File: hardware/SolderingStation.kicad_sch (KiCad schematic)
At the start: 10 parts, among them J1 AC Screw Terminal, J2 Iron Encoder, J3 Hot Air Encoder, J4 OLED, J5 STM32 SWD, J6 ESP UART, J7 STM BOOT, J8 +5V

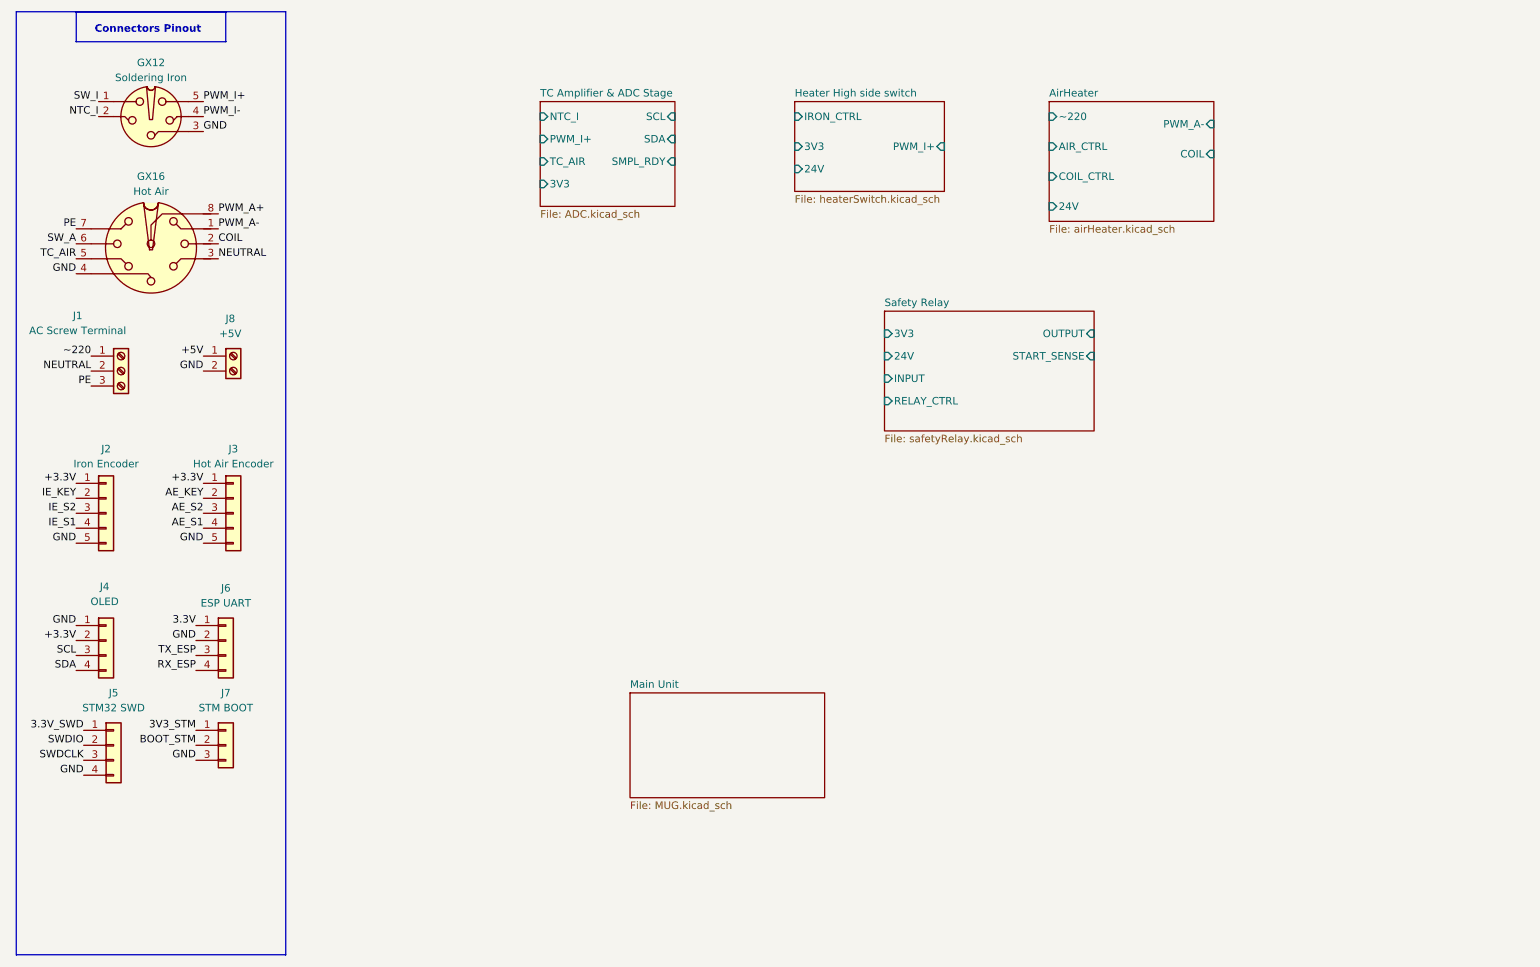
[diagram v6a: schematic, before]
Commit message: mvp
features:
	Logic Power Supply
	Safety Relay
	Main Unit
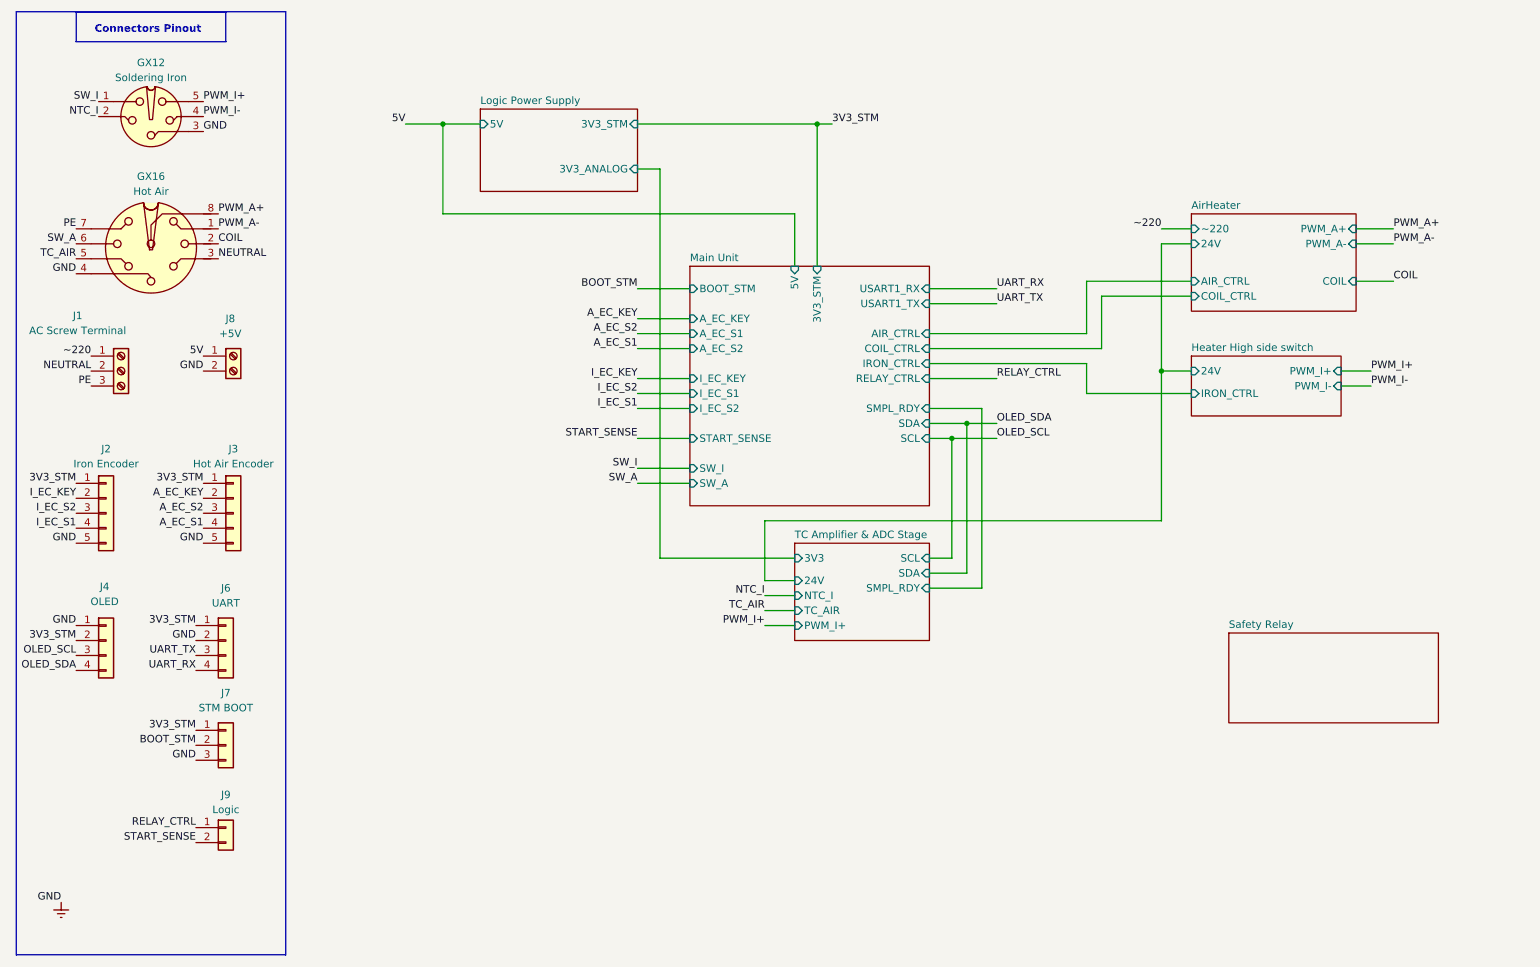
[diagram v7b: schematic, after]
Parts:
- removed J5: STM32 SWD, symbol Connector_Generic:Conn_01x04
- added J9: Logic, symbol Connector_Generic:Conn_01x02
- J6: value ESP UART -> UART
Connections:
- net +3.3V is gone; now on net 3V3_STM: J2.1 (Pin_1), J3.1 (Pin_1), J4.2 (Pin_2)
- net 3.3V is gone; now on net 3V3_STM: J6.1 (Pin_1)
- net +5V renamed 5V
- net AE_KEY renamed A_EC_KEY
- net AE_S1 renamed A_EC_S1
- net AE_S2 renamed A_EC_S2
- net GND renamed GNDREF
- net IE_KEY renamed I_EC_KEY
- net IE_S1 renamed I_EC_S1
- net IE_S2 renamed I_EC_S2
- net RX_ESP renamed UART_RX
- net SCL renamed OLED_SCL
- net SDA renamed OLED_SDA
- net TX_ESP renamed UART_TX
- new net RELAY_CTRL: J9.1 (Pin_1)
- new net START_SENSE: J9.2 (Pin_2)
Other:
- added sheet Logic Power Supply (LogicPowerSupply.kicad_sch)
- sheet AirHeater ports: added PWM_A+; removed none
- sheet Heater High side switch ports: added PWM_I-; removed 3V3
- sheet Main Unit ports: added 3V3_STM, 5V, AIR_CTRL, A_EC_KEY, A_EC_S1, A_EC_S2, BOOT_STM, COIL_CTRL, IRON_CTRL, I_EC_KEY, I_EC_S1, I_EC_S2, RELAY_CTRL, SCL, SDA, SMPL_RDY, START_SENSE, SW_A, SW_I, USART1_RX, USART1_TX; removed none
- sheet Safety Relay ports: added none; removed 24V, 3V3, INPUT, OUTPUT, RELAY_CTRL, START_SENSE
- sheet TC Amplifier & ADC Stage ports: added 24V; removed none

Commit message: starting pcb
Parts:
- added J12: SWD, Connector_PinHeader_2.54mm:PinHeader_1x04_P2.54mm_Vertical, symbol Connector_Generic:Conn_01x04
- GX12: footprint (none) -> SolderingStationLib:GX-12-5
- GX16: footprint (none) -> SolderingStationLib:GX-16-8
- J1: footprint (none) -> TerminalBlock:TerminalBlock_MaiXu_MX126-5.0-03P_1x03_P5.00mm
- J2, J3: footprint (none) -> Connector_PinHeader_2.54mm:PinHeader_1x05_P2.54mm_Vertical
- J4, J6: footprint (none) -> Connector_PinHeader_2.54mm:PinHeader_1x04_P2.54mm_Vertical
- J7: footprint (none) -> Connector_PinHeader_2.54mm:PinHeader_1x03_P2.54mm_Vertical
- J8: footprint (none) -> TerminalBlock:TerminalBlock_MaiXu_MX126-5.0-02P_1x02_P5.00mm
- J9: footprint (none) -> Connector_PinHeader_2.54mm:PinHeader_1x02_P2.54mm_Vertical
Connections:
- net 3V3_STM: now also J12.1 (Pin_1)
- net GNDREF: now also J12.4 (Pin_4)
- new net SWCLK: J12.3 (Pin_3)
- new net SWDIO: J12.2 (Pin_2)
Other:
- sheet Main Unit ports: added SWCLK, SWDIO; removed none
- title: ESP32 Soldering Iron -> STM32 Soldering Iron
